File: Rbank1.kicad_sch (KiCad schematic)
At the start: 118 parts, among them K10 TQ2-5, K11 TQ2-5, K12 TQ2-5, K13 TQ2-5, K5 TQ2-5, K6 TQ2-5, K7 TQ2-5, K8 TQ2-5, K9 TQ2-5, Q1 2N2222, Q2 2N2222, Q3 2N2222, Q4 2N2222, Q5 2N2222, Q6 2N2222, Q7 2N2222, Q8 2N2222, Q9 2N2222

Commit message: First try to fit electronic on PCB
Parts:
- removed D1, D10, D11, D12, D17, D2, D3, D4, D9: LED, LED_THT:LED_D3.0mm_Clear, symbol Device:LED
- removed R1, R10, R11, R12, R17, R2, R3, R4, R9: 220, Resistor_THT:R_Axial_DIN0309_L9.0mm_D3.2mm_P12.70mm_Horizontal, symbol Device:R_US
- TP1, TP10, TP11, TP12, TP13, TP14, TP15, TP16, TP2, TP3, TP4, TP5, TP6, TP7, TP8, TP9: footprint Connector_Pin:Pin_D1.2mm_L11.3mm_W3.0mm_Flat -> Connector_Pin:Pin_D1.0mm_L10.0mm
- renumbered D5 to D1, D6 to D2, D7 to D3, D8 to D4, D13 to D5, D14 to D6, D15 to D7, D16 to D8, D18 to D9, K5 to K1, K6 to K2, K7 to K3, K8 to K4, K9 to K5, K10 to K6, K11 to K7, K12 to K8, K13 to K9, R5 to R1, R6 to R2, R7 to R3, R8 to R4, R13 to R5, R14 to R6, R15 to R7, R16 to R8, R18 to R9

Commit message: backup 1 bank done
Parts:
- removed D1, D2, D3, D4, D5, D6, D7, D8, D9: 1N4148, Diode_THT:D_DO-35_SOD27_P7.62mm_Horizontal, symbol Diode:1N4148
- removed NT23: NT16_H, NetTie:NetTie-2_THT_Pad1.0mm, symbol Device:NetTie_2
- removed NT24: NT17_H, NetTie:NetTie-2_THT_Pad1.0mm, symbol Device:NetTie_2
- removed NT25: NT14_CH, NetTie:NetTie-2_THT_Pad1.0mm, symbol Device:NetTie_2
- removed NT26: NT15_CH, NetTie:NetTie-2_THT_Pad1.0mm, symbol Device:NetTie_2
- removed NT27: NT16_CH, NetTie:NetTie-2_THT_Pad1.0mm, symbol Device:NetTie_2
- removed NT28: NT17_CH, NetTie:NetTie-2_THT_Pad1.0mm, symbol Device:NetTie_2
- removed NT29: NT14_L, NetTie:NetTie-2_THT_Pad1.0mm, symbol Device:NetTie_2
- removed NT30: NT15_L, NetTie:NetTie-2_THT_Pad1.0mm, symbol Device:NetTie_2
- removed NT31: NT16_L, NetTie:NetTie-2_THT_Pad1.0mm, symbol Device:NetTie_2
- removed NT32: NT17_L, NetTie:NetTie-2_THT_Pad1.0mm, symbol Device:NetTie_2
- removed NT33: NT14_CL, NetTie:NetTie-2_THT_Pad1.0mm, symbol Device:NetTie_2
- removed NT34: NT15_CL, NetTie:NetTie-2_THT_Pad1.0mm, symbol Device:NetTie_2
- removed NT35: NT16_CL, NetTie:NetTie-2_THT_Pad1.0mm, symbol Device:NetTie_2
- removed NT36: NT17_CL, NetTie:NetTie-2_THT_Pad1.0mm, symbol Device:NetTie_2
- removed NT37: NT14_D, NetTie:NetTie-2_THT_Pad1.0mm, symbol Device:NetTie_2
- removed NT38: NT15_D, NetTie:NetTie-2_THT_Pad1.0mm, symbol Device:NetTie_2
- removed NT39: NT16_D, NetTie:NetTie-2_THT_Pad1.0mm, symbol Device:NetTie_2
- removed NT40: NT17_D, NetTie:NetTie-2_THT_Pad1.0mm, symbol Device:NetTie_2
- removed NT41, NT44: NT1S_RL, NetTie:NetTie-2_THT_Pad1.0mm, symbol Device:NetTie_2
- removed NT42: NT1S_CH, NetTie:NetTie-2_THT_Pad1.0mm, symbol Device:NetTie_2
- removed NT43: NT1S_NH, NetTie:NetTie-2_THT_Pad1.0mm, symbol Device:NetTie_2
- removed NT45: NT1S_CL, NetTie:NetTie-2_THT_Pad1.0mm, symbol Device:NetTie_2
- removed NT46: NT1S_L1, NetTie:NetTie-2_THT_Pad1.0mm, symbol Device:NetTie_2
- removed NT47: NT1S_D, NetTie:NetTie-2_THT_Pad1.0mm, symbol Device:NetTie_2
- removed Q1, Q2, Q3, Q4, Q5, Q6, Q7, Q8, Q9: 2N2222, Package_TO_SOT_THT:TO-92_Inline, symbol Transistor_BJT:2N3904
- removed R1, R2, R3, R4, R5, R6, R7, R8, R9: 10K, Resistor_THT:R_Axial_DIN0309_L9.0mm_D3.2mm_P12.70mm_Horizontal, symbol Device:R_US
- NT1: value NT10_H -> NT10_CH; footprint NetTie:NetTie-2_THT_Pad1.0mm -> NetTie:NetTie-2_Front1.0mm
- NT10: value NT11_L -> NT15_CH; footprint NetTie:NetTie-2_THT_Pad1.0mm -> NetTie:NetTie-2_Front1.0mm
- NT11: value NT12_L -> NT16_CH; footprint NetTie:NetTie-2_THT_Pad1.0mm -> NetTie:NetTie-2_Front1.0mm
- NT12: value NT13_L -> NT17_CH; footprint NetTie:NetTie-2_THT_Pad1.0mm -> NetTie:NetTie-2_Front1.0mm
- NT13: value NT10_CL -> NT14_CL; footprint NetTie:NetTie-2_THT_Pad1.0mm -> NetTie:NetTie-2_Front1.0mm
- NT14: value NT11_CL -> NT15_CL; footprint NetTie:NetTie-2_THT_Pad1.0mm -> NetTie:NetTie-2_Front1.0mm
- NT15: value NT12_CL -> NT16_CL; footprint NetTie:NetTie-2_THT_Pad1.0mm -> NetTie:NetTie-2_Front1.0mm
- NT16: value NT13_CL -> NT17_CL; footprint NetTie:NetTie-2_THT_Pad1.0mm -> NetTie:NetTie-2_Front1.0mm
- NT17: value NT10_D -> NT1S_RL; footprint NetTie:NetTie-2_THT_Pad1.0mm -> NetTie:NetTie-2_Front1.0mm
- NT18: value NT11_D -> NT1S_CH; footprint NetTie:NetTie-2_THT_Pad1.0mm -> NetTie:NetTie-2_Front1.0mm
- NT19: value NT12_D -> NT1S_NH; footprint NetTie:NetTie-2_THT_Pad1.0mm -> NetTie:NetTie-2_Front1.0mm
- NT2: value NT11_H -> NT11_CH; footprint NetTie:NetTie-2_THT_Pad1.0mm -> NetTie:NetTie-2_Front1.0mm
- NT20: value NT13_D -> NT1S_RL; footprint NetTie:NetTie-2_THT_Pad1.0mm -> NetTie:NetTie-2_Front1.0mm
- NT21: value NT14_H -> NT1S_CL; footprint NetTie:NetTie-2_THT_Pad1.0mm -> NetTie:NetTie-2_Front1.0mm
- NT22: value NT15_H -> NT1S_L1; footprint NetTie:NetTie-2_THT_Pad1.0mm -> NetTie:NetTie-2_Front1.0mm
- NT3: value NT12_H -> NT12_CH; footprint NetTie:NetTie-2_THT_Pad1.0mm -> NetTie:NetTie-2_Front1.0mm
- NT4: value NT13_H -> NT13_CH; footprint NetTie:NetTie-2_THT_Pad1.0mm -> NetTie:NetTie-2_Front1.0mm
- NT5: value NT10_CH -> NT10_CL; footprint NetTie:NetTie-2_THT_Pad1.0mm -> NetTie:NetTie-2_Front1.0mm
- NT6: value NT11_CH -> NT11_CL; footprint NetTie:NetTie-2_THT_Pad1.0mm -> NetTie:NetTie-2_Front1.0mm
- NT7: value NT12_CH -> NT12_CL; footprint NetTie:NetTie-2_THT_Pad1.0mm -> NetTie:NetTie-2_Front1.0mm
- NT8: value NT13_CH -> NT13_CL; footprint NetTie:NetTie-2_THT_Pad1.0mm -> NetTie:NetTie-2_Front1.0mm
- NT9: value NT10_L -> NT14_CH; footprint NetTie:NetTie-2_THT_Pad1.0mm -> NetTie:NetTie-2_Front1.0mm
- TP1, TP10, TP11, TP12, TP13, TP14, TP15, TP16, TP2, TP3, TP4, TP5, TP6, TP7, TP8, TP9: footprint Connector_Pin:Pin_D1.0mm_L10.0mm -> Connector_Pin:Pin_D0.9mm_L10.0mm_W2.4mm_FlatFork
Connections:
- net B10_CH: now also NT1.2; no longer NT5.2
- net B10_CL: now also NT5.2; no longer NT13.2
- net B10_H: now also K1.7; no longer NT1.2
- net B10_L: now also K1.4; no longer NT9.2
- net B11_CH: now also NT2.2; no longer NT6.2
- net B11_CL: now also NT6.2; no longer NT14.2
- net B11_H: now also K2.7; no longer NT2.2
- net B11_L: now also K2.4; no longer NT10.2
- net B12_CH: now also NT3.2; no longer NT7.2
- net B12_CL: now also NT7.2; no longer NT15.2
- net B12_H: now also K3.7; no longer NT3.2
- net B12_L: now also K3.4; no longer NT11.2
- net B13_CH: now also NT4.2; no longer NT8.2
- net B13_CL: now also NT8.2; no longer NT16.2
- net B13_H: now also K4.7; no longer NT4.2
- net B13_L: now also K4.4; no longer NT12.2
- net B14_CH: now also NT9.2
- net B14_CL: now also NT13.2
- net B14_H: now also K5.7; no longer NT21.2
- net B14_L: now also K5.4
- net B15_CH: now also NT10.2
- net B15_CL: now also NT14.2
- net B15_H: now also K6.7; no longer NT22.2
- net B15_L: now also K6.4
- net B16_CH: now also NT11.2
- net B16_CL: now also NT15.2
- net B16_H: now also K7.7
- net B16_L: now also K7.4
- net B17_CH: now also NT12.2
- net B17_CL: now also NT16.2
- net B17_H: now also K8.7
- net B17_L: now also K8.4
- net B1_COM_H: now also NT18.1
- net B1_COM_L: now also NT21.1
- net BANK1_BUS_H: now also NT19.2, NT20.2, NT5.1, NT6.1, NT7.1, NT8.1
- net BANK1_BUS_L: now also NT1.1, NT10.1, NT11.1, NT12.1, NT17.2, NT2.1, NT22.2, NT3.1, NT4.1, NT9.1; no longer NT5.1, NT6.1, NT7.1, NT8.1
- net B16_R: now reaches K7.10
- net B17_R: now reaches K8.10
- net B15_R: now reaches K6.10
- net at NT22.1: now also K9.2; no longer K6.7
- net at K9.9: now also NT19.1
- net B1S_R: now reaches K9.10
- net at K2.10: no longer NT18.1
- net at K9.4: now also NT20.1
- net B13_R: now reaches K4.10
- net B13_R: no longer NT20.1
- net at K9.7: now also NT17.1
- net B10_R: now reaches K1.10
- net B10_R: no longer NT17.1
- net B12_R: now reaches K3.10
- net B12_R: no longer NT19.1
- net B14_R: now reaches K5.10
- net at NT18.2: now also K9.8
- net at K9.3: now also NT21.2

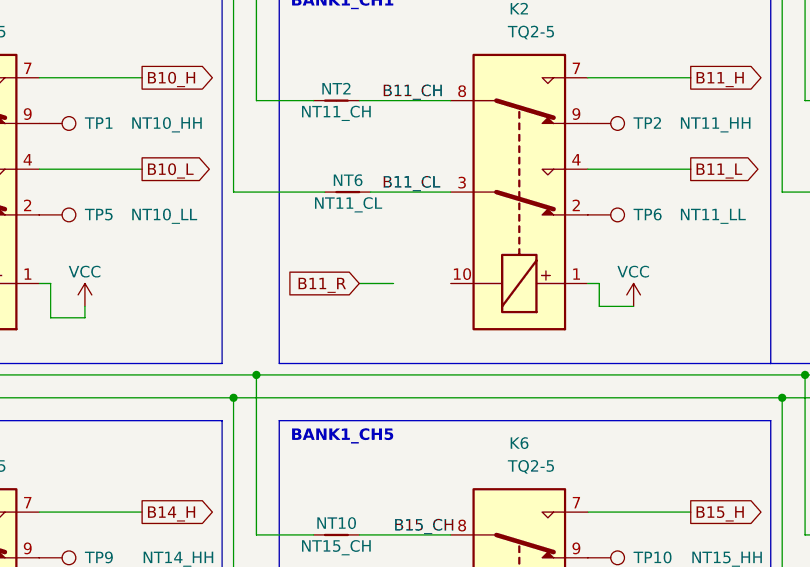
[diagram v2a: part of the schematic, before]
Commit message: half PCB completed
FTS io controller PCB
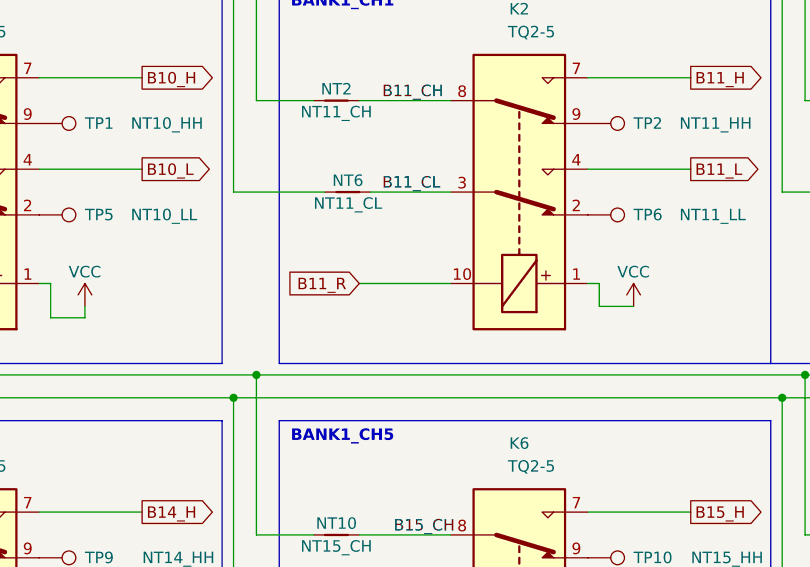
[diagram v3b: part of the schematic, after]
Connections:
- net B11_R: now also K2.10
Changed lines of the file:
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@@
     (stroke (width 0) (type default) (color 0 0 0 0))
   )
-  (wire (pts (xy 91.44 52.07) (xy 95.25 52.07))
+  (wire (pts (xy 91.44 52.07) (xy 101.6 52.07))
     (stroke (width 0) (type default) (color 0 0 0 0))
   )

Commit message: PCB Completed
PCB completed but final verification not completed
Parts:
- TP1, TP10, TP11, TP12, TP13, TP14, TP15, TP16, TP2, TP3, TP4, TP5, TP6, TP7, TP8, TP9: footprint Connector_Pin:Pin_D0.9mm_L10.0mm_W2.4mm_FlatFork -> TestPoint:TestPoint_THTPad_D1.5mm_Drill0.7mm
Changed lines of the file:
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@@
       (effects (font (size 1.27 1.27)) (justify left))
     )
-    (property "Footprint" "Connector_Pin:Pin_D0.9mm_L10.0mm_W2.4mm_FlatFork" (id 2) (at 55.88 97.79 0)
+    (property "Footprint" "TestPoint:TestPoint_THTPad_D1.5mm_Drill0.7mm" (id 2) (at 55.88 97.79 0)
       (effects (font (size 1.27 1.27)) hide)
     )
@@
       (effects (font (size 1.27 1.27)) (justify left))
     )
-    (property "Footprint" "Connector_Pin:Pin_D0.9mm_L10.0mm_W2.4mm_FlatFork" (id 2) (at 238.76 87.63 0)
+    (property "Footprint" "TestPoint:TestPoint_THTPad_D1.5mm_Drill0.7mm" (id 2) (at 238.76 87.63 0)
       (effects (font (size 1.27 1.27)) hide)
     )
@@
       (effects (font (size 1.27 1.27)) (justify left))
     )
-    (property "Footprint" "Connector_Pin:Pin_D0.9mm_L10.0mm_W2.4mm_FlatFork" (id 2) (at 177.8 87.63 0)
+    (property "Footprint" "TestPoint:TestPoint_THTPad_D1.5mm_Drill0.7mm" (id 2) (at 177.8 87.63 0)
       (effects (font (size 1.27 1.27)) hide)
     )
@@
       (effects (font (size 1.27 1.27)) (justify left))
     )
-    (property "Footprint" "Connector_Pin:Pin_D0.9mm_L10.0mm_W2.4mm_FlatFork" (id 2) (at 116.84 39.37 0)
+    (property "Footprint" "TestPoint:TestPoint_THTPad_D1.5mm_Drill0.7mm" (id 2) (at 116.84 39.37 0)
       (effects (font (size 1.27 1.27)) hide)
     )
@@
       (effects (font (size 1.27 1.27)) (justify left))
     )
-    (property "Footprint" "Connector_Pin:Pin_D0.9mm_L10.0mm_W2.4mm_FlatFork" (id 2) (at 177.8 97.79 0)
+    (property "Footprint" "TestPoint:TestPoint_THTPad_D1.5mm_Drill0.7mm" (id 2) (at 177.8 97.79 0)
       (effects (font (size 1.27 1.27)) hide)
     )
@@
       (effects (font (size 1.27 1.27)) (justify left))
     )
-    (property "Footprint" "Connector_Pin:Pin_D0.9mm_L10.0mm_W2.4mm_FlatFork" (id 2) (at 238.76 39.37 0)
+    (property "Footprint" "TestPoint:TestPoint_THTPad_D1.5mm_Drill0.7mm" (id 2) (at 238.76 39.37 0)
       (effects (font (size 1.27 1.27)) hide)
     )
@@
       (effects (font (size 1.27 1.27)) (justify left))
     )
-    (property "Footprint" "Connector_Pin:Pin_D0.9mm_L10.0mm_W2.4mm_FlatFork" (id 2) (at 116.84 49.53 0)
+    (property "Footprint" "TestPoint:TestPoint_THTPad_D1.5mm_Drill0.7mm" (id 2) (at 116.84 49.53 0)
       (effects (font (size 1.27 1.27)) hide)
     )
@@
       (effects (font (size 1.27 1.27)) (justify left))
     )
-    (property "Footprint" "Connector_Pin:Pin_D0.9mm_L10.0mm_W2.4mm_FlatFork" (id 2) (at 238.76 97.79 0)
+    (property "Footprint" "TestPoint:TestPoint_THTPad_D1.5mm_Drill0.7mm" (id 2) (at 238.76 97.79 0)
       (effects (font (size 1.27 1.27)) hide)
     )
@@
       (effects (font (size 1.27 1.27)) (justify left))
     )
-    (property "Footprint" "Connector_Pin:Pin_D0.9mm_L10.0mm_W2.4mm_FlatFork" (id 2) (at 238.76 49.53 0)
+    (property "Footprint" "TestPoint:TestPoint_THTPad_D1.5mm_Drill0.7mm" (id 2) (at 238.76 49.53 0)
       (effects (font (size 1.27 1.27)) hide)
     )
@@
       (effects (font (size 1.27 1.27)) (justify left))
     )
-    (property "Footprint" "Connector_Pin:Pin_D0.9mm_L10.0mm_W2.4mm_FlatFork" (id 2) (at 116.84 97.79 0)
+    (property "Footprint" "TestPoint:TestPoint_THTPad_D1.5mm_Drill0.7mm" (id 2) (at 116.84 97.79 0)
       (effects (font (size 1.27 1.27)) hide)
     )
@@
       (effects (font (size 1.27 1.27)) (justify left))
     )
-    (property "Footprint" "Connector_Pin:Pin_D0.9mm_L10.0mm_W2.4mm_FlatFork" (id 2) (at 55.88 39.37 0)
+    (property "Footprint" "TestPoint:TestPoint_THTPad_D1.5mm_Drill0.7mm" (id 2) (at 55.88 39.37 0)
       (effects (font (size 1.27 1.27)) hide)
     )
@@
       (effects (font (size 1.27 1.27)) (justify left))
     )
-    (property "Footprint" "Connector_Pin:Pin_D0.9mm_L10.0mm_W2.4mm_FlatFork" (id 2) (at 177.8 49.53 0)
+    (property "Footprint" "TestPoint:TestPoint_THTPad_D1.5mm_Drill0.7mm" (id 2) (at 177.8 49.53 0)
       (effects (font (size 1.27 1.27)) hide)
     )
@@
       (effects (font (size 1.27 1.27)) (justify left))
     )
-    (property "Footprint" "Connector_Pin:Pin_D0.9mm_L10.0mm_W2.4mm_FlatFork" (id 2) (at 55.88 49.53 0)
+    (property "Footprint" "TestPoint:TestPoint_THTPad_D1.5mm_Drill0.7mm" (id 2) (at 55.88 49.53 0)
       (effects (font (size 1.27 1.27)) hide)
     )
@@
       (effects (font (size 1.27 1.27)) (justify left))
     )
-    (property "Footprint" "Connector_Pin:Pin_D0.9mm_L10.0mm_W2.4mm_FlatFork" (id 2) (at 116.84 87.63 0)
+    (property "Footprint" "TestPoint:TestPoint_THTPad_D1.5mm_Drill0.7mm" (id 2) (at 116.84 87.63 0)
       (effects (font (size 1.27 1.27)) hide)
     )
@@
       (effects (font (size 1.27 1.27)) (justify left))
     )
-    (property "Footprint" "Connector_Pin:Pin_D0.9mm_L10.0mm_W2.4mm_FlatFork" (id 2) (at 55.88 87.63 0)
+    (property "Footprint" "TestPoint:TestPoint_THTPad_D1.5mm_Drill0.7mm" (id 2) (at 55.88 87.63 0)
       (effects (font (size 1.27 1.27)) hide)
     )
@@
       (effects (font (size 1.27 1.27)) (justify left))
     )
-    (property "Footprint" "Connector_Pin:Pin_D0.9mm_L10.0mm_W2.4mm_FlatFork" (id 2) (at 177.8 39.37 0)
-      (effects (font (size 1.27 1.27)) hide)
-    )
+    (property "Footprint" "TestPoint:TestPoint_THTPad_D1.5mm_Drill0.7mm" (id 2) (at 177.8 39.37 0)
+      (effects (font (size 1.27 1.27)) hide)
+    )
